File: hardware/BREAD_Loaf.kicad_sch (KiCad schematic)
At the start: 32 parts, among them J2 THING_PLUS_LOGICAL, J6 PPPC101LGBN-RC, Q1 BSS138, Q2 BSS138, Q3 BSS138, U1 AP63205WU-7, U1 LTC4311ISC6-TRMPBF, U3 PCA9306

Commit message: added art and cleared erc errors
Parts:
- HS1: footprint SparkFun-Fuse:Thermal Pad -> KML-Custom:Thermal Pad
- J2: footprint SparkFun-RF:ESP_THING_PLUS -> SparkFun-Board:ThingPlus
- JP1, JP2, JP3, JP4: footprint SparkFun-Jumper:SMT-JUMPER_2_NC_TRACE_SILK -> SparkFun-Jumper:Jumper_2_NC_Trace
- ST1: footprint SparkFun-Hardware:STAND-OFF -> SparkFun-Hardware:Standoff
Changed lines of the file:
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@@
 			)
 		)
-		(property "Footprint" "SparkFun-Fuse:Thermal Pad"
+		(property "Footprint" "KML-Custom:Thermal Pad"
 			(at 69.85 49.8348 0)
 			(effects
@@
 			)
 		)
-		(property "Footprint" "SparkFun-Jumper:SMT-JUMPER_2_NC_TRACE_SILK"
+		(property "Footprint" "SparkFun-Jumper:Jumper_2_NC_Trace"
 			(at 192.024 117.602 0)
 			(effects
@@
 			)
 		)
-		(property "Footprint" "SparkFun-Hardware:STAND-OFF"
+		(property "Footprint" "SparkFun-Hardware:Standoff"
 			(at 22.86 45.72 0)
 			(effects
@@
 			)
 		)
-		(property "Footprint" "SparkFun-Hardware:STAND-OFF"
+		(property "Footprint" "SparkFun-Hardware:Standoff"
 			(at 19.05 45.72 0)
 			(effects
@@
 			)
 		)
-		(property "Footprint" "SparkFun-RF:ESP_THING_PLUS"
+		(property "Footprint" "SparkFun-Board:ThingPlus"
 			(at 44.45 105.41 0)
 			(effects
@@
 			)
 		)
-		(property "Footprint" "SparkFun-Jumper:SMT-JUMPER_2_NC_TRACE_SILK"
+		(property "Footprint" "SparkFun-Jumper:Jumper_2_NC_Trace"
 			(at 192.024 83.058 0)
 			(effects
@@
 			)
 		)
-		(property "Footprint" "SparkFun-Jumper:SMT-JUMPER_2_NC_TRACE_SILK"
+		(property "Footprint" "SparkFun-Jumper:Jumper_2_NC_Trace"
 			(at 192.024 105.918 0)
 			(effects
@@
 			)
 		)
-		(property "Footprint" "SparkFun-Jumper:SMT-JUMPER_2_NC_TRACE_SILK"
+		(property "Footprint" "SparkFun-Jumper:Jumper_2_NC_Trace"
 			(at 192.024 94.742 0)
 			(effects

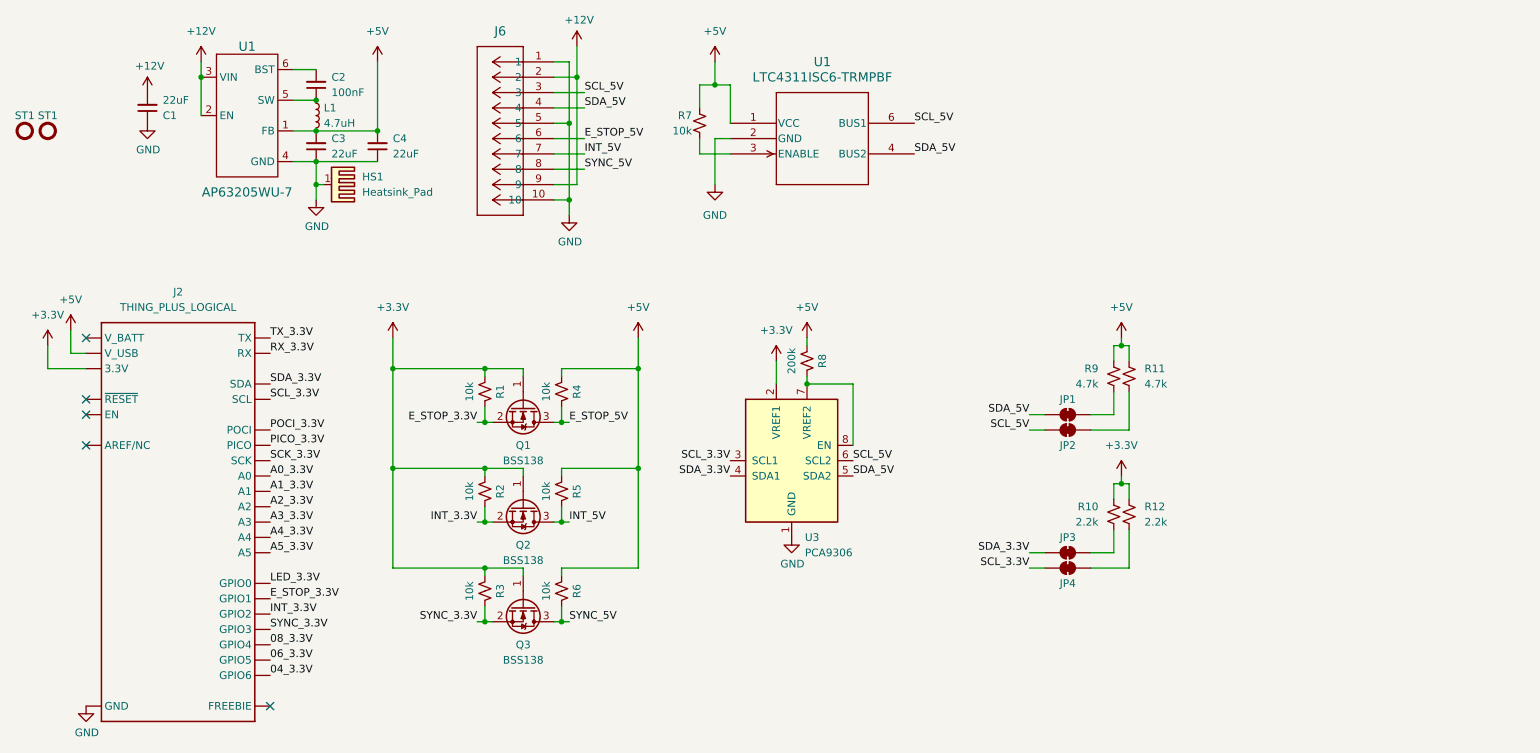
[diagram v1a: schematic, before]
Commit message: updated to remove i2c shifter and optimized layout
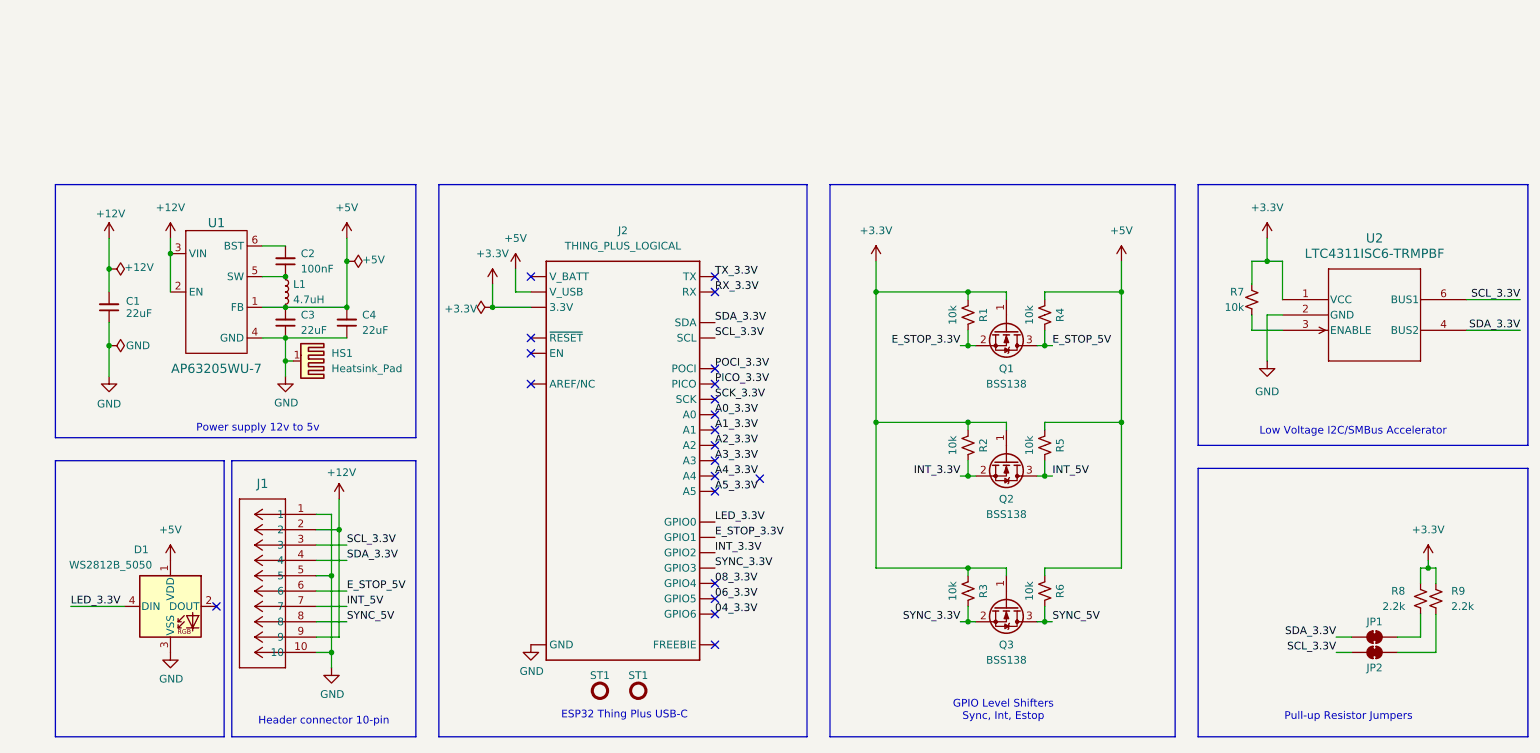
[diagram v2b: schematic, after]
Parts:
- removed JP1, JP2: ~, SparkFun-Jumper:Jumper_2_NC_Trace, symbol SparkFun-Jumper:SolderJumper_2_Bridged
- removed R11, R9: 4.7k, Resistor_SMD:R_0603_1608Metric, symbol Device:R_Small_US
- removed R8: 200k, Resistor_SMD:R_0603_1608Metric, symbol Device:R_Small_US
- removed U3: PCA9306, Package_SO:SSOP-8_2.95x2.8mm_P0.65mm, symbol Interface:PCA9306
- added D1: WS2812B_5050, SparkFun-LED:WS2812-5050-4PIN, symbol SparkFun-LED:WS2812B_5050
- renumbered J6 to J1, JP3 to JP1, JP4 to JP2, R10 to R8, R12 to R9, U1 to U2
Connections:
- net SCL_5V is gone; now on net SCL_3.3V: J1.3, U2.6 (BUS1)
- net SDA_5V is gone; now on net SDA_3.3V: J1.4, U2.4 (BUS2)
- net +3.3V: now also R7.1, U2.1 (VCC)
- net +5V: now also D1.1 (VDD); no longer R7.1, U2.1 (VCC)
- net GND: now also D1.3 (VSS)
- net LED_3.3V: now also D1.4 (DIN)
- no-connect marks 5 -> 21
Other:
- note added: "ESP32 Thing Plus USB-C"
- note added: "GPIO Level Shifters Sync, Int, Estop"
- note added: "Header connector 10-pin"
- note added: "Low Voltage I2C/SMBus Accelerator"
- note added: "Power supply 12v to 5v"
- note added: "Pull-up Resistor Jumpers"
- moved on the sheet: C1, C2, C3, C4, HS1, J1, J2, JP1, JP2, L1, Q1, Q2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
